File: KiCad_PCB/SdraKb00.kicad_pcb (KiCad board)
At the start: 2 copper layers, 85.2 x 83.9 mm, 75 parts, among them J1 AVR-ISP-6, SW00 SW_Push_45deg, SW01 SW_Push_45deg, SW02 SW_Push_45deg, SW03 RotaryEncoder_Switch, SW10 SW_Push_45deg, SW11 SW_Push_45deg, SW12 SW_Push_45deg, SW13 SW_Push_45deg, SW20 SW_Push_45deg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

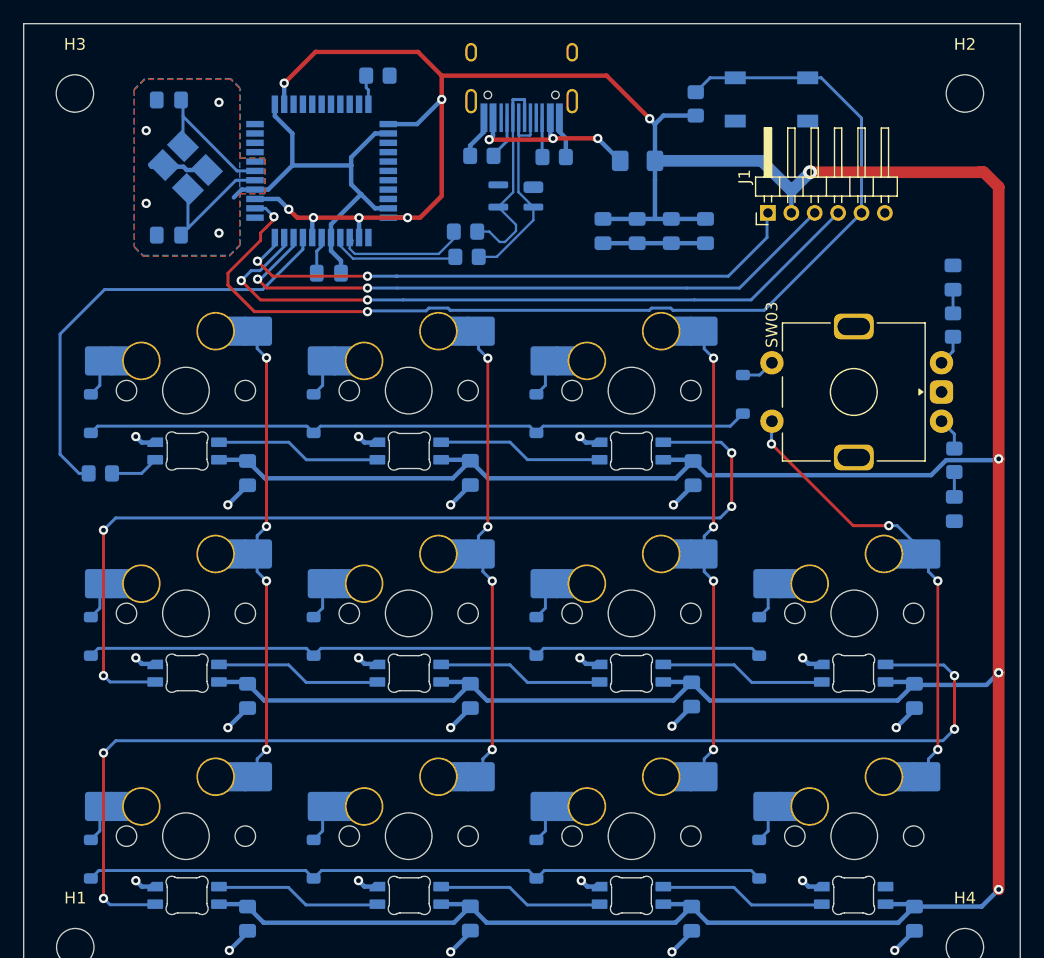
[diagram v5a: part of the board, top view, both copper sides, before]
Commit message: Routing switch matrix.
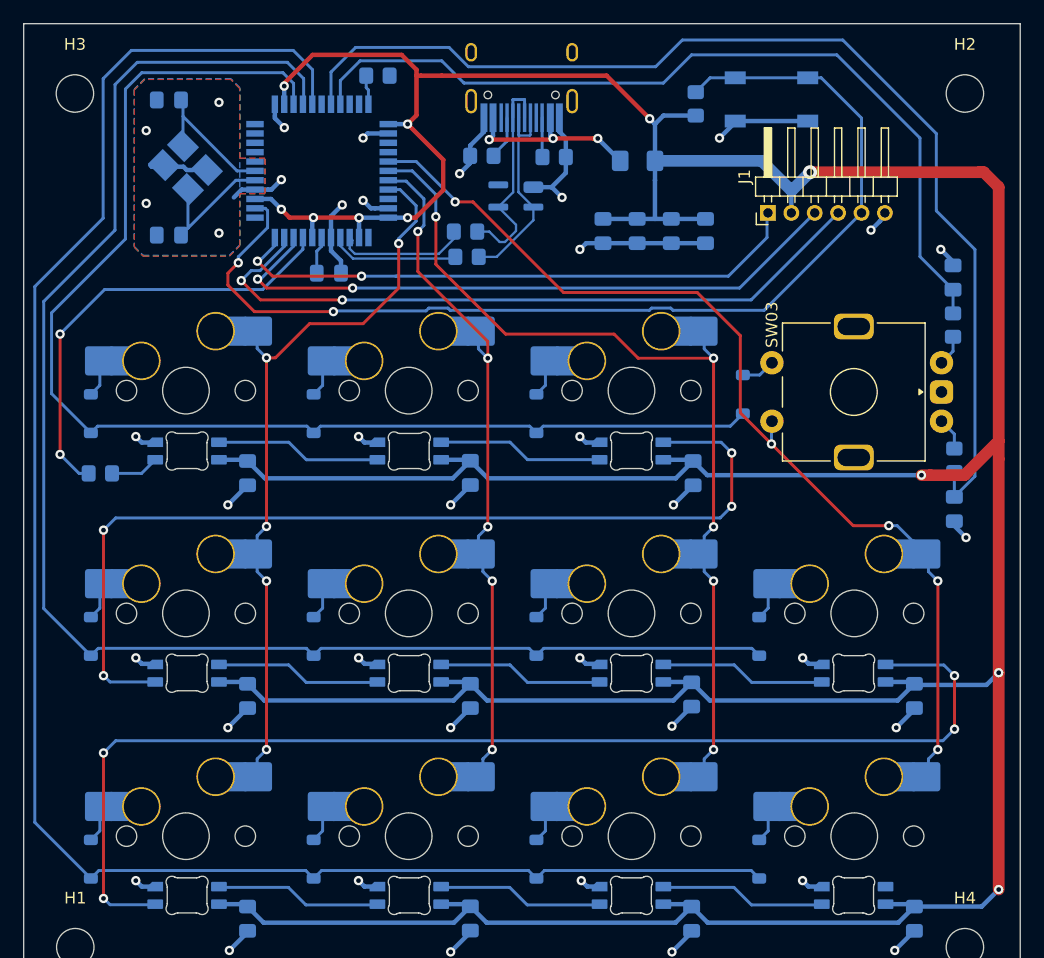
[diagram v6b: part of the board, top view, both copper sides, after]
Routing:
- net Row2: track 58.8 -> 154.4 mm
- net Enc_A: track 2.13 -> 95.6 mm
- net Row1: track 58.7 -> 131.5 mm
- net Enc_B: track 2.03 -> 73.2 mm
- net Row0: track 57.4 -> 107.9 mm
- net Col3: track 38.7 -> 85.5 mm, vias 4 -> 5
- net Col2: track 39.4 -> 77.4 mm, vias 4 -> 5
- net Col0: track 39.4 -> 63.8 mm, vias 4 -> 5
- net Col1: track 40.0 -> 60.1 mm, vias 4 -> 5
- net GND: track 101.9 -> 108.5 mm, vias 26 -> 38
- net +5V: track 421.9 -> 418.6 mm
- net RGB_CHAIN: vias 0 -> 2

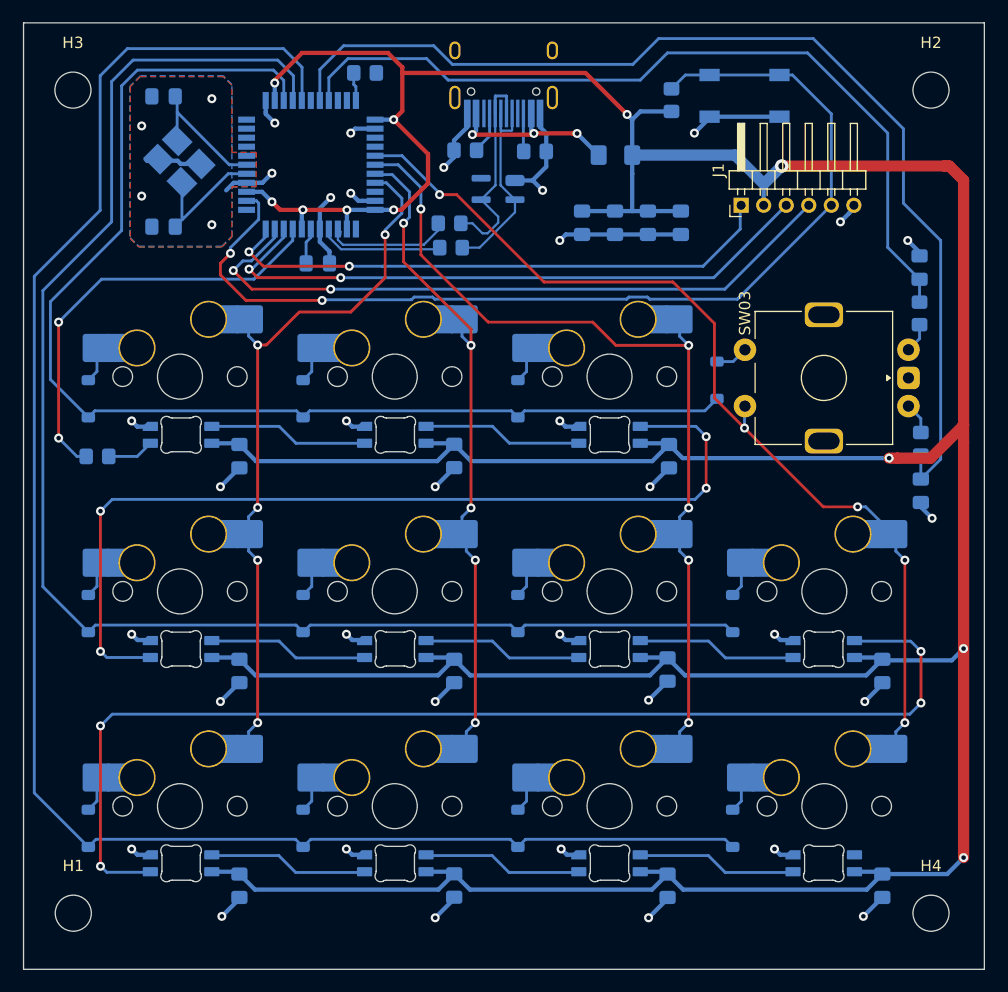
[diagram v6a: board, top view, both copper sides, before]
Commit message: Cutting rounded corner edges.
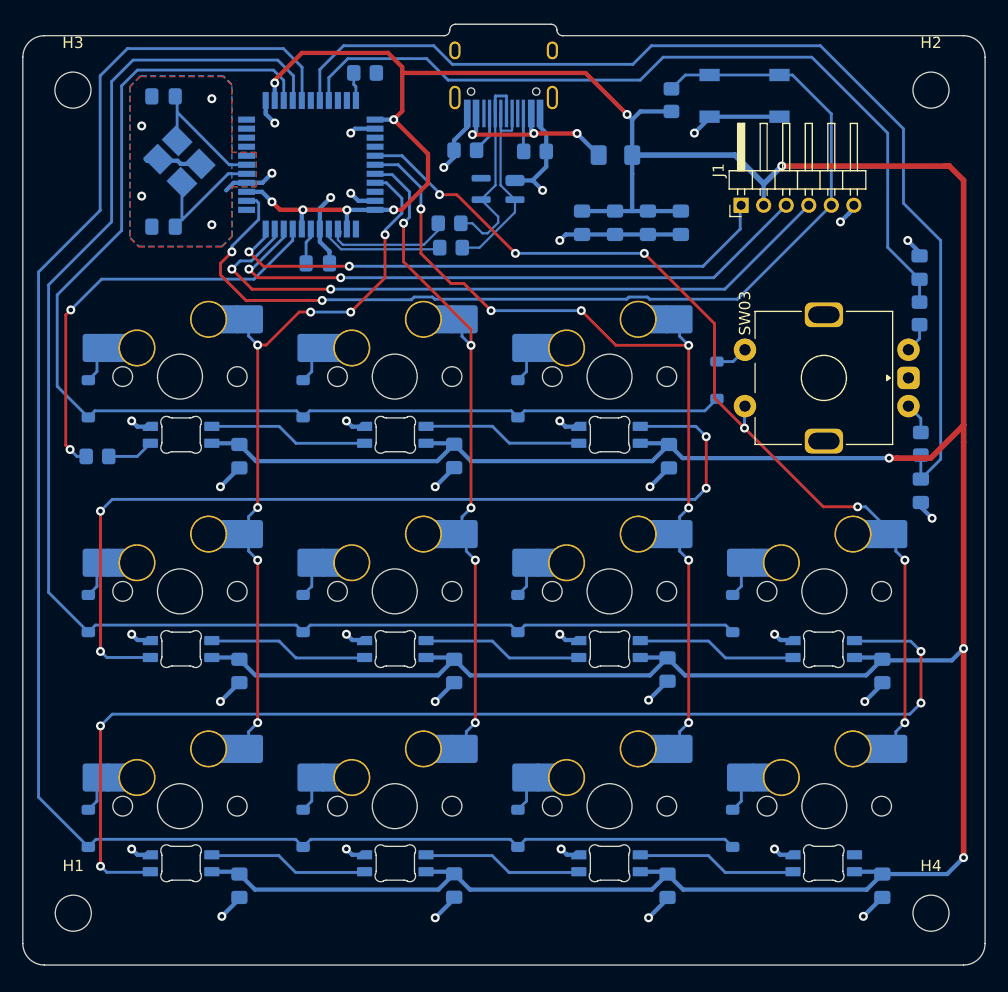
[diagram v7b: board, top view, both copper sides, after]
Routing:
- net RGB_CHAIN: track 38.2 -> 37.7 mm
- net Enc_A: track 95.6 -> 95.1 mm
- net Col2: track 77.4 -> 77.3 mm, vias 5 -> 7
- net Col3: vias 5 -> 7
- net Col0: vias 5 -> 7
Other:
- board size 85.2 x 83.9 mm -> 85.3 x 83.4 mm
